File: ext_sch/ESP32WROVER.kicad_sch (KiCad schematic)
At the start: 3 parts, among them U3 ESP32-WROVER

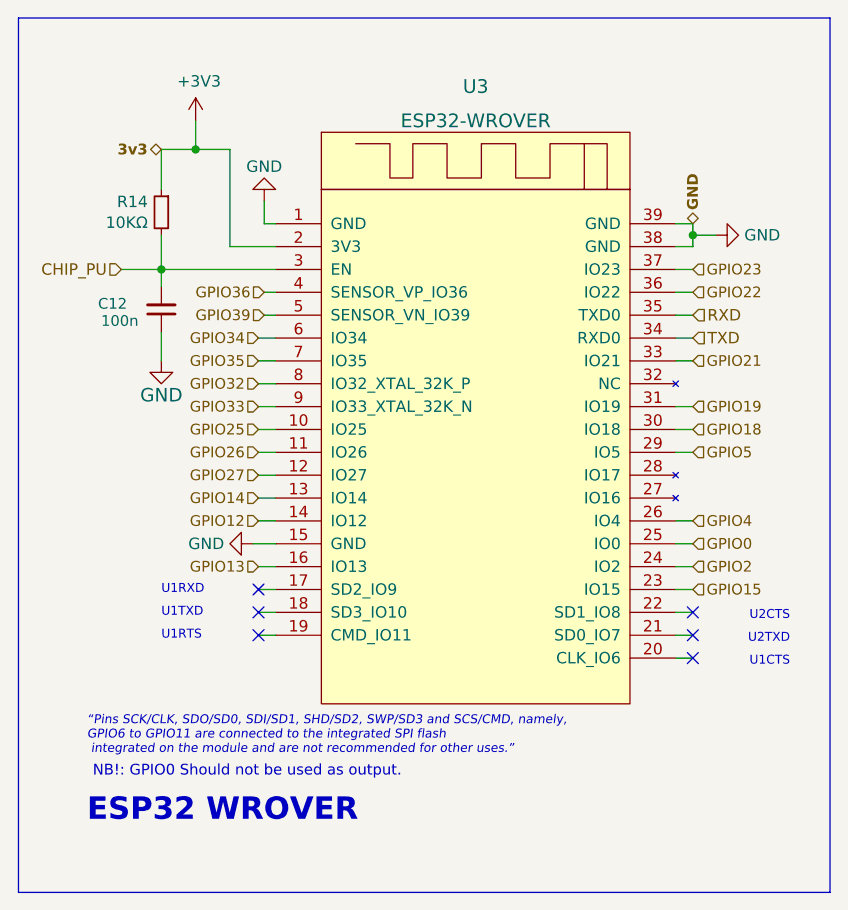
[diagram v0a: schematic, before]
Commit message: Rev04 in the works. New changes include; New DCDC buck, two new connectors, replaced WS-diodes, removed err-diode
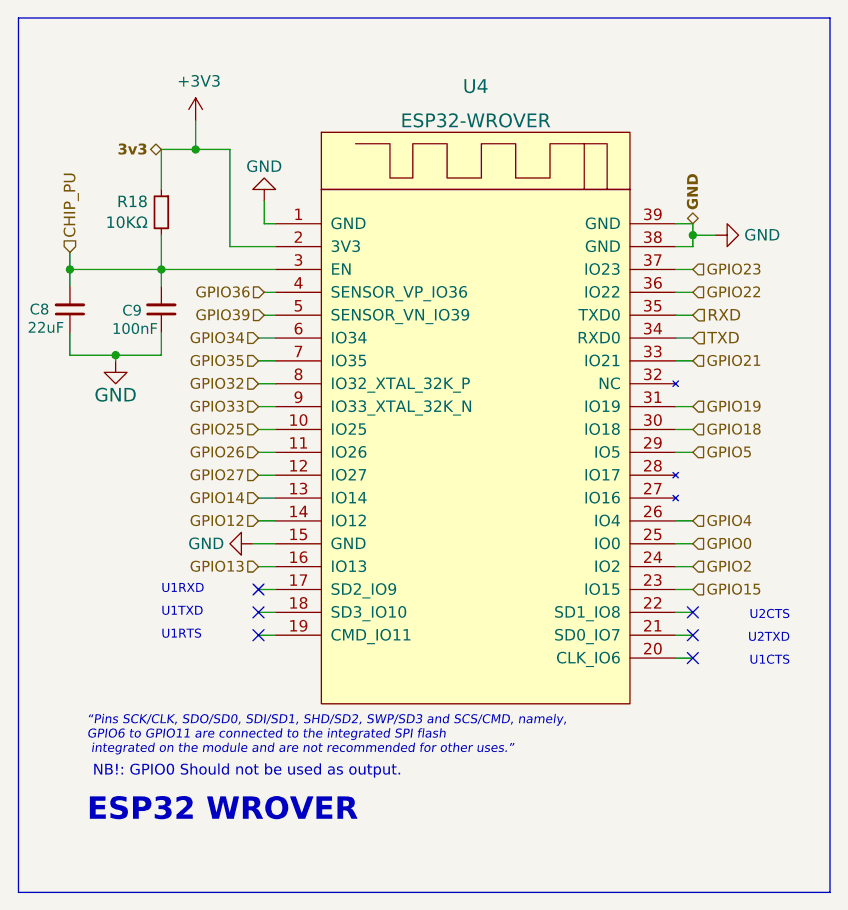
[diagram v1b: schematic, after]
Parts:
- added C8: 22uF, Capacitor_SMD:C_0603_1608Metric, symbol Device:C_Small
- C9: renamed from C12; value 100n -> 100nF
- renumbered R14 to R18, U3 to U4
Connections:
- net CHIP_PU: now also C8.2
- net GND: now also C8.1
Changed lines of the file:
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@@
 (kicad_sch (version 20211123) (generator eeschema)
   (paper "A4")
+  (junction (at 24.765 51.435) (diameter 0) (color 0 0 0 0)
+  )
   (junction (at 88.9 38.1) (diameter 0) (color 0 0 0 0)
   )
   (junction (at 29.845 41.91) (diameter 0) (color 0 0 0 0)
+  )
+  (junction (at 19.685 41.91) (diameter 0) (color 0 0 0 0)
   )
   (junction (at 33.655 28.575) (diameter 0) (color 0 0 0 0)
@@
     (stroke (width 0) (type default) (color 0 0 0 0))
   )
+  (wire (pts (xy 24.765 51.435) (xy 29.845 51.435))
+    (stroke (width 0) (type default) (color 0 0 0 0))
+  )
+  (wire (pts (xy 19.685 48.895) (xy 19.685 51.435))
+    (stroke (width 0) (type default) (color 0 0 0 0))
+  )
   (polyline (pts (xy 104.14 13.97) (xy 13.97 13.97))
     (stroke (width 0) (type default) (color 0 0 0 0))
@@
     (stroke (width 0) (type default) (color 0 0 0 0))
   )
+  (wire (pts (xy 19.685 41.91) (xy 29.845 41.91))
+    (stroke (width 0) (type default) (color 0 0 0 0))
+  )
   (wire (pts (xy 88.9 38.1) (xy 88.9 39.37))
     (stroke (width 0) (type default) (color 0 0 0 0))
   )
-  (wire (pts (xy 29.845 41.91) (xy 25.4 41.91))
+  (wire (pts (xy 19.685 41.91) (xy 19.685 43.815))
     (stroke (width 0) (type default) (color 0 0 0 0))
   )
@@
     (stroke (width 0) (type default) (color 0 0 0 0))
   )
-  (wire (pts (xy 29.845 48.895) (xy 29.845 52.07))
+  (wire (pts (xy 29.845 48.895) (xy 29.845 51.435))
     (stroke (width 0) (type default) (color 0 0 0 0))
   )
@@
     (stroke (width 0) (type default) (color 0 0 0 0))
   )
+  (wire (pts (xy 24.765 51.435) (xy 24.765 52.07))
+    (stroke (width 0) (type default) (color 0 0 0 0))
+  )
   (wire (pts (xy 42.545 44.45) (xy 41.275 44.45))
     (stroke (width 0) (type default) (color 0 0 0 0))
@@
     (stroke (width 0) (type default) (color 0 0 0 0))
   )
+  (wire (pts (xy 19.685 51.435) (xy 24.765 51.435))
+    (stroke (width 0) (type default) (color 0 0 0 0))
+  )
   (wire (pts (xy 33.655 28.575) (xy 29.845 28.575))
     (stroke (width 0) (type default) (color 0 0 0 0))
@@
   )
   (wire (pts (xy 40.64 52.07) (xy 42.545 52.07))
+    (stroke (width 0) (type default) (color 0 0 0 0))
+  )
+  (wire (pts (xy 19.685 40.005) (xy 19.685 41.91))
     (stroke (width 0) (type default) (color 0 0 0 0))
   )
@@
     (effects (font (size 1.1938 1.1938)) (justify left))
   )
-  (hierarchical_label "CHIP_PU" (shape input) (at 25.4 41.91 180)
-    (effects (font (size 1.27 1.27)) (justify right))
+  (hierarchical_label "CHIP_PU" (shape input) (at 19.685 40.005 90)
+    (effects (font (size 1.27 1.27)) (justify left))
   )
   (hierarchical_label "GPIO35" (shape input) (at 40.64 52.07 180)
@@
     (effects (font (size 1.1938 1.1938)) (justify left))
   )
-  (symbol (lib_id "power:GND") (at 29.845 52.07 0) (unit 1)
-    (in_bom yes) (on_board yes)
-    (property "Reference" "#SUPPLY05" (id 0) (at 29.845 52.07 0)
-      (effects (font (size 1.27 1.27)) hide)
-    )
-    (property "Value" "GND" (id 1) (at 29.845 55.88 0)
+  (symbol (lib_id "power:GND") (at 24.765 52.07 0) (unit 1)
+    (in_bom yes) (on_board yes)
+    (property "Reference" "#SUPPLY04" (id 0) (at 24.765 52.07 0)
+      (effects (font (size 1.27 1.27)) hide)
+    )
+    (property "Value" "GND" (id 1) (at 24.765 55.88 0)
       (effects (font (size 1.4986 1.4986)))
     )
-    (property "Footprint" "" (id 2) (at 29.845 52.07 0)
-      (effects (font (size 1.27 1.27)) hide)
-    )
-    (property "Datasheet" "" (id 3) (at 29.845 52.07 0)
+    (property "Footprint" "" (id 2) (at 24.765 52.07 0)
+      (effects (font (size 1.27 1.27)) hide)
+    )
+    (property "Datasheet" "" (id 3) (at 24.765 52.07 0)
       (effects (font (size 1.27 1.27)) hide)
     )
@@
   (symbol (lib_id "Device:C_Small") (at 29.845 46.355 180) (unit 1)
     (in_bom yes) (on_board yes)
-    (property "Reference" "C12" (id 0) (at 26.035 45.72 0)
+    (property "Reference" "C9" (id 0) (at 27.686 46.482 0)
       (effects (font (size 1.1938 1.1938)) (justify left))
     )
-    (property "Value" "100n" (id 1) (at 27.305 47.625 0)
+    (property "Value" "100nF" (id 1) (at 29.464 48.514 0)
       (effects (font (size 1.1938 1.1938)) (justify left))
     )
@@
   (symbol (lib_id "power:+3V3") (at 33.655 25.4 0) (unit 1)
     (in_bom yes) (on_board yes)
-    (property "Reference" "#PWR044" (id 0) (at 33.655 29.21 0)
+    (property "Reference" "#PWR048" (id 0) (at 33.655 29.21 0)
       (effects (font (size 1.27 1.27)) hide)
     )
@@
   (symbol (lib_id "power:GND") (at 41.275 34.29 180) (unit 1)
     (in_bom yes) (on_board yes)
-    (property "Reference" "#PWR046" (id 0) (at 41.275 27.94 0)
+    (property "Reference" "#PWR050" (id 0) (at 41.275 27.94 0)
       (effects (font (size 1.27 1.27)) hide)
     )
@@
   (symbol (lib_id "power:GND") (at 40.005 72.39 270) (unit 1)
     (in_bom yes) (on_board yes)
-    (property "Reference" "#PWR045" (id 0) (at 33.655 72.39 0)
+    (property "Reference" "#PWR049" (id 0) (at 33.655 72.39 0)
       (effects (font (size 1.27 1.27)) hide)
     )
@@
   (symbol (lib_id "power:GND") (at 91.44 38.1 90) (unit 1)
     (in_bom yes) (on_board yes)
-    (property "Reference" "#PWR047" (id 0) (at 97.79 38.1 0)
+    (property "Reference" "#PWR051" (id 0) (at 97.79 38.1 0)
       (effects (font (size 1.27 1.27)) hide)
     )
@@
   (symbol (lib_id "Device:R_Small") (at 29.845 35.56 0) (mirror y) (unit 1)
     (in_bom yes) (on_board yes)
-    (property "Reference" "R14" (id 0) (at 28.3464 34.3916 0)
+    (property "Reference" "R18" (id 0) (at 28.3464 34.3916 0)
       (effects (font (size 1.27 1.27)) (justify left))
     )
@@
     (pin "2")
   )
+  (symbol (lib_id "Device:C_Small") (at 19.685 46.355 180) (unit 1)
+    (in_bom yes) (on_board yes)
+    (property "Reference" "C8" (id 0) (at 17.399 46.355 0)
+      (effects (font (size 1.1938 1.1938)) (justify left))
+    )
+    (property "Value" "22uF" (id 1) (at 19.05 48.387 0)
+      (effects (font (size 1.1938 1.1938)) (justify left))
+    )
+    (property "Footprint" "Capacitor_SMD:C_0603_1608Metric" (id 2) (at 19.685 46.355 0)
+      (effects (font (size 1.27 1.27)) hide)
+    )
+    (property "Datasheet" "" (id 3) (at 19.685 46.355 0)
+      (effects (font (size 1.27 1.27)) hide)
+    )
+    (property "LCSC" "C30926" (id 4) (at 19.685 46.355 90)
+      (effects (font (size 1.27 1.27)) hide)
+    )
+    (pin "1")
+    (pin "2")
+  )
   (symbol (lib_id "Lib:ESP32-WROVER") (at 65.405 55.88 0) (unit 1)
     (in_bom yes) (on_board yes) (fields_autoplaced)
-    (property "Reference" "U3" (id 0) (at 64.77 21.59 0)
+    (property "Reference" "U4" (id 0) (at 64.77 21.59 0)
       (effects (font (size 1.524 1.524)))
     )

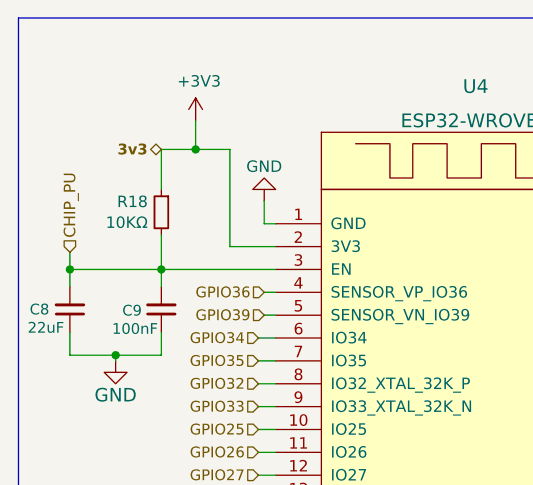
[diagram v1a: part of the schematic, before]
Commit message: Lastest revised files. Loads more DC protection now, thanks to @feelfreelinux
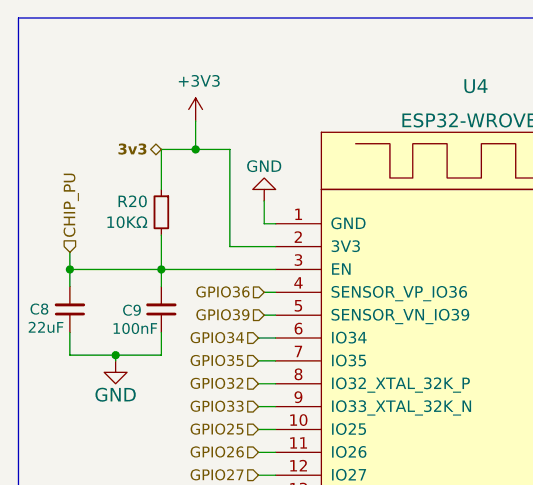
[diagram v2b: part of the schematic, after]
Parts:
- renumbered R18 to R20
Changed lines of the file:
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@@
   (symbol (lib_id "power:+3V3") (at 33.655 25.4 0) (unit 1)
     (in_bom yes) (on_board yes)
-    (property "Reference" "#PWR048" (id 0) (at 33.655 29.21 0)
+    (property "Reference" "#PWR049" (id 0) (at 33.655 29.21 0)
       (effects (font (size 1.27 1.27)) hide)
     )
@@
   (symbol (lib_id "power:GND") (at 41.275 34.29 180) (unit 1)
     (in_bom yes) (on_board yes)
-    (property "Reference" "#PWR050" (id 0) (at 41.275 27.94 0)
+    (property "Reference" "#PWR051" (id 0) (at 41.275 27.94 0)
       (effects (font (size 1.27 1.27)) hide)
     )
@@
   (symbol (lib_id "power:GND") (at 40.005 72.39 270) (unit 1)
     (in_bom yes) (on_board yes)
-    (property "Reference" "#PWR049" (id 0) (at 33.655 72.39 0)
+    (property "Reference" "#PWR050" (id 0) (at 33.655 72.39 0)
       (effects (font (size 1.27 1.27)) hide)
     )
@@
   (symbol (lib_id "power:GND") (at 91.44 38.1 90) (unit 1)
     (in_bom yes) (on_board yes)
-    (property "Reference" "#PWR051" (id 0) (at 97.79 38.1 0)
+    (property "Reference" "#PWR052" (id 0) (at 97.79 38.1 0)
       (effects (font (size 1.27 1.27)) hide)
     )
@@
   (symbol (lib_id "Device:R_Small") (at 29.845 35.56 0) (mirror y) (unit 1)
     (in_bom yes) (on_board yes)
-    (property "Reference" "R18" (id 0) (at 28.3464 34.3916 0)
+    (property "Reference" "R20" (id 0) (at 28.3464 34.3916 0)
       (effects (font (size 1.27 1.27)) (justify left))
     )

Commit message: feat: new schematic, adjust LCSC part numbers
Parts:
- C8: LCSC C30926 -> C106222
- R20: LCSC C98220 -> C25804
- U4: Digikey 1965-ESP32-WROVER-E-N16R8CT-ND -> (none); TME (none) -> ESP32-WROVER-E-16
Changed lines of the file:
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@@
       (effects (font (size 1.27 1.27)) hide)
     )
-    (property "LCSC" "C98220" (id 4) (at 29.845 35.56 0)
+    (property "LCSC" "C25804" (id 4) (at 29.845 35.56 0)
       (effects (font (size 1.27 1.27)) hide)
     )
@@
       (effects (font (size 1.27 1.27)) hide)
     )
-    (property "LCSC" "C30926" (id 4) (at 19.685 46.355 90)
+    (property "LCSC" "C106222" (id 4) (at 19.685 46.355 90)
       (effects (font (size 1.27 1.27)) hide)
     )
@@
       (effects (font (size 1.524 1.524)) hide)
     )
-    (property "Datasheet" "" (id 3) (at 76.835 63.5 0)
+    (property "Datasheet" "https://www.tme.eu/Document/491a1d31a59e7fa917e66fab6313b5e3/esp32-wrover-e.pdf" (id 3) (at 76.835 63.5 0)
       (effects (font (size 1.524 1.524)) hide)
     )
-    (property "Digikey" "1965-ESP32-WROVER-E-N16R8CT-ND" (id 4) (at 65.405 55.88 0)
+    (property "TME" "ESP32-WROVER-E-16" (id 4) (at 65.405 55.88 0)
       (effects (font (size 1.27 1.27)) hide)
     )

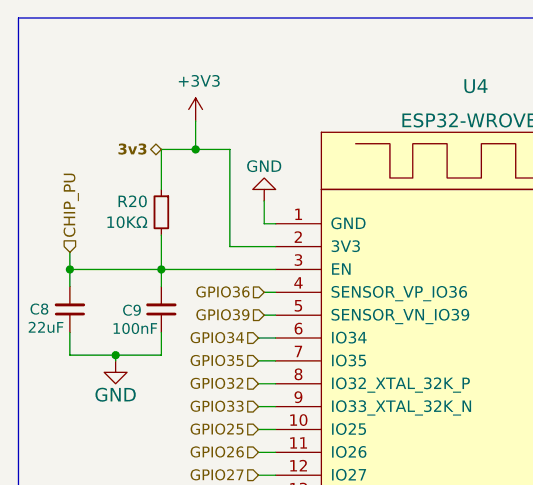
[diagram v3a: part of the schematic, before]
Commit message: Rerouted a couple of small things pr. @feelfreelinux request
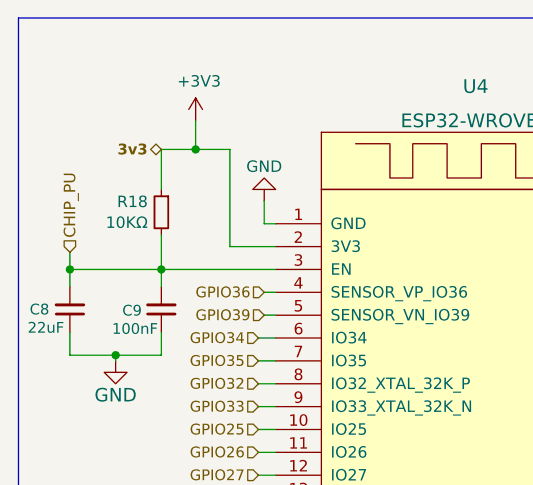
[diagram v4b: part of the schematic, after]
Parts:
- renumbered R20 to R18
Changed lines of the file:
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@@
   (symbol (lib_id "power:+3V3") (at 33.655 25.4 0) (unit 1)
     (in_bom yes) (on_board yes)
-    (property "Reference" "#PWR049" (id 0) (at 33.655 29.21 0)
+    (property "Reference" "#PWR048" (id 0) (at 33.655 29.21 0)
       (effects (font (size 1.27 1.27)) hide)
     )
@@
   (symbol (lib_id "power:GND") (at 41.275 34.29 180) (unit 1)
     (in_bom yes) (on_board yes)
-    (property "Reference" "#PWR051" (id 0) (at 41.275 27.94 0)
+    (property "Reference" "#PWR050" (id 0) (at 41.275 27.94 0)
       (effects (font (size 1.27 1.27)) hide)
     )
@@
   (symbol (lib_id "power:GND") (at 40.005 72.39 270) (unit 1)
     (in_bom yes) (on_board yes)
-    (property "Reference" "#PWR050" (id 0) (at 33.655 72.39 0)
+    (property "Reference" "#PWR049" (id 0) (at 33.655 72.39 0)
       (effects (font (size 1.27 1.27)) hide)
     )
@@
   (symbol (lib_id "power:GND") (at 91.44 38.1 90) (unit 1)
     (in_bom yes) (on_board yes)
-    (property "Reference" "#PWR052" (id 0) (at 97.79 38.1 0)
+    (property "Reference" "#PWR051" (id 0) (at 97.79 38.1 0)
       (effects (font (size 1.27 1.27)) hide)
     )
@@
   (symbol (lib_id "Device:R_Small") (at 29.845 35.56 0) (mirror y) (unit 1)
     (in_bom yes) (on_board yes)
-    (property "Reference" "R20" (id 0) (at 28.3464 34.3916 0)
+    (property "Reference" "R18" (id 0) (at 28.3464 34.3916 0)
       (effects (font (size 1.27 1.27)) (justify left))
     )

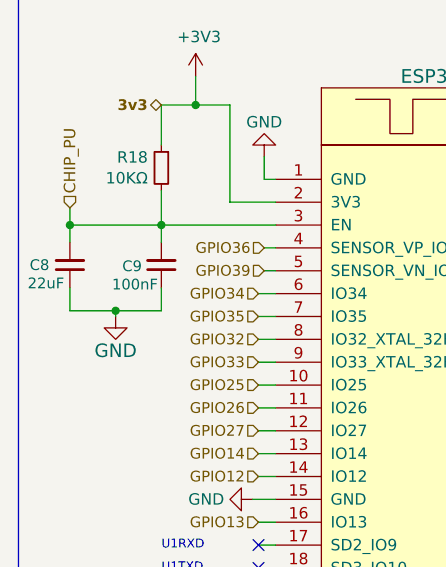
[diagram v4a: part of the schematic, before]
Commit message: Added missing partsnumbers and ordered latest rev. PCBS
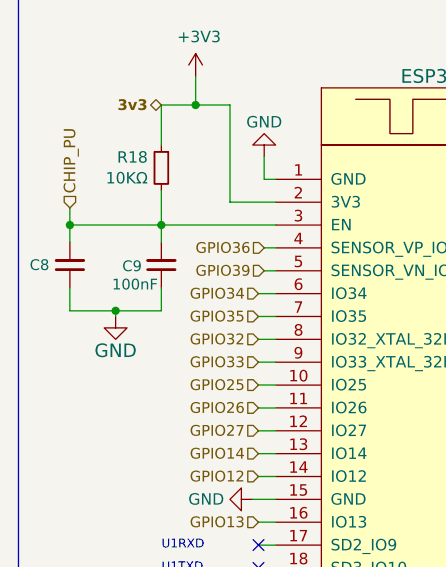
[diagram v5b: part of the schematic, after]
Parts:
- C8: value 22uF -> (none); footprint Capacitor_SMD:C_0603_1608Metric -> (none)
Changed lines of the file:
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@@
       (effects (font (size 1.1938 1.1938)) (justify left))
     )
-    (property "Value" "22uF" (id 1) (at 19.05 48.387 0)
+    (property "Value" "" (id 1) (at 19.05 48.387 0)
       (effects (font (size 1.1938 1.1938)) (justify left))
     )
-    (property "Footprint" "Capacitor_SMD:C_0603_1608Metric" (id 2) (at 19.685 46.355 0)
+    (property "Footprint" "" (id 2) (at 19.685 46.355 0)
       (effects (font (size 1.27 1.27)) hide)
     )

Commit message: Minor changes. Flipped Q2 PMOS and fixed some silkscreening
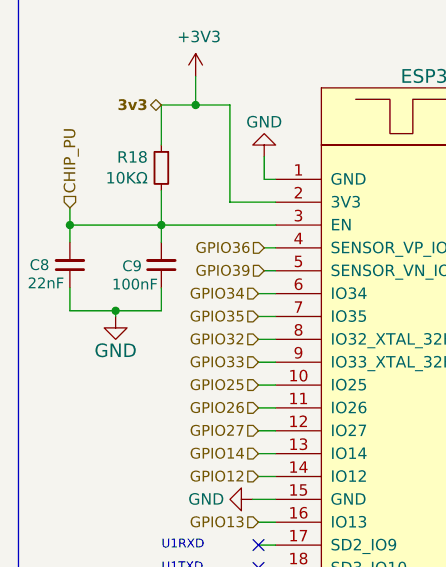
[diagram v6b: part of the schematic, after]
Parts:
- C8: value (none) -> 22nF; footprint (none) -> Capacitor_SMD:C_0603_1608Metric
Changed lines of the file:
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@@
       (effects (font (size 1.1938 1.1938)) (justify left))
     )
-    (property "Value" "" (id 1) (at 19.05 48.387 0)
+    (property "Value" "22nF" (id 1) (at 19.05 48.387 0)
       (effects (font (size 1.1938 1.1938)) (justify left))
     )
-    (property "Footprint" "" (id 2) (at 19.685 46.355 0)
+    (property "Footprint" "Capacitor_SMD:C_0603_1608Metric" (id 2) (at 19.685 46.355 0)
       (effects (font (size 1.27 1.27)) hide)
     )
